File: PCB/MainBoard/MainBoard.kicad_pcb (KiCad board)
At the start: 2 copper layers, 100 x 100 mm, 73 parts, among them J10 Conn_01x06_Socket, J11 Conn_01x06_Socket, J12 Conn_01x04_Socket, J14 Conn_01x03_Socket, J17 Conn_01x02_Socket, J18 Conn_01x04_Socket, J19 Conn_01x04_Socket, J20 Conn_01x04_Socket, J21 Conn_01x02_Socket, J4 Conn_01x02_Socket, J5 Conn_01x03_Socket, J6 Conn_01x03_Socket, J7 Conn_01x03_Socket, J8 Conn_01x02_Socket, J9 Conn_01x02_Socket, SW1 SW_Push, U1 TPS56339DDC, U2 TPS56339DDC, U3 STM32F103C8Tx, U4 CD74HC00_N_14, U5 TPS56339DDC, U6 CD74HC00_N_14

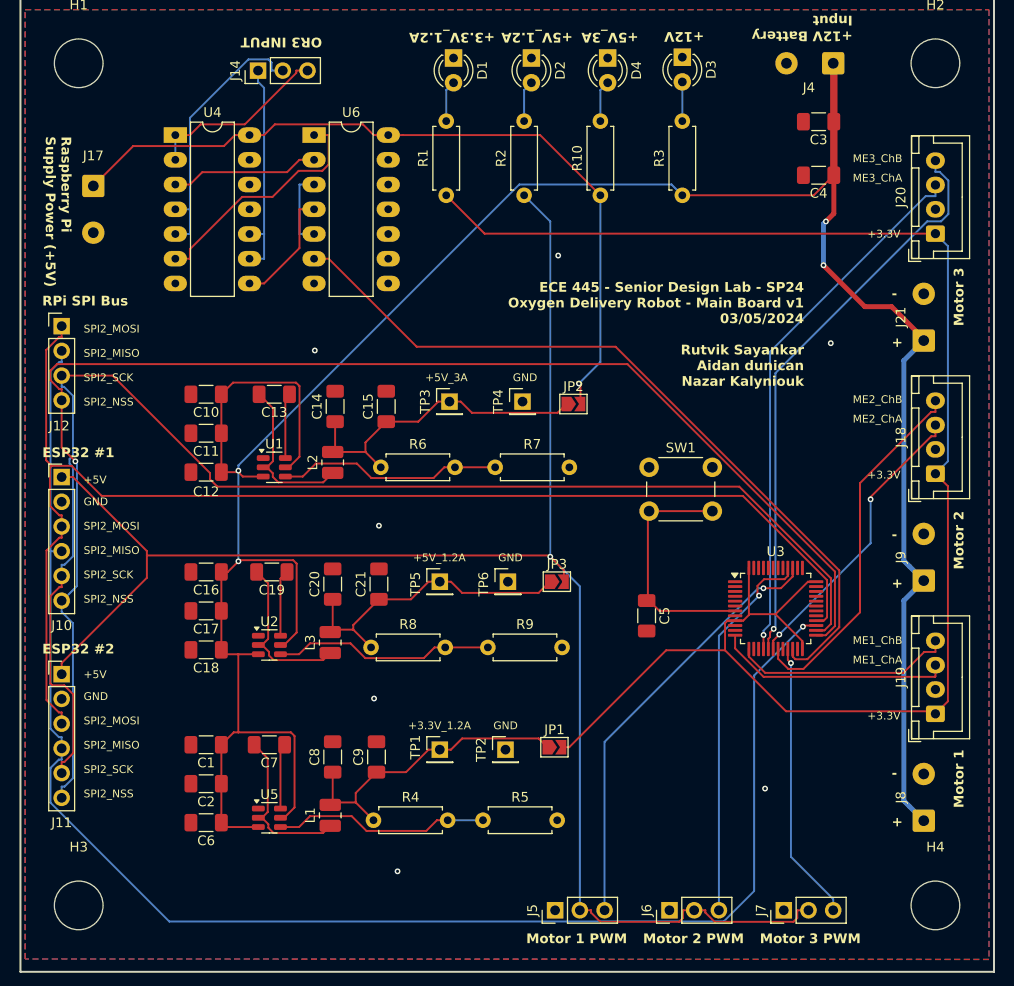
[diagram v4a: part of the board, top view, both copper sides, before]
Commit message: Updated PCB and passed DRC
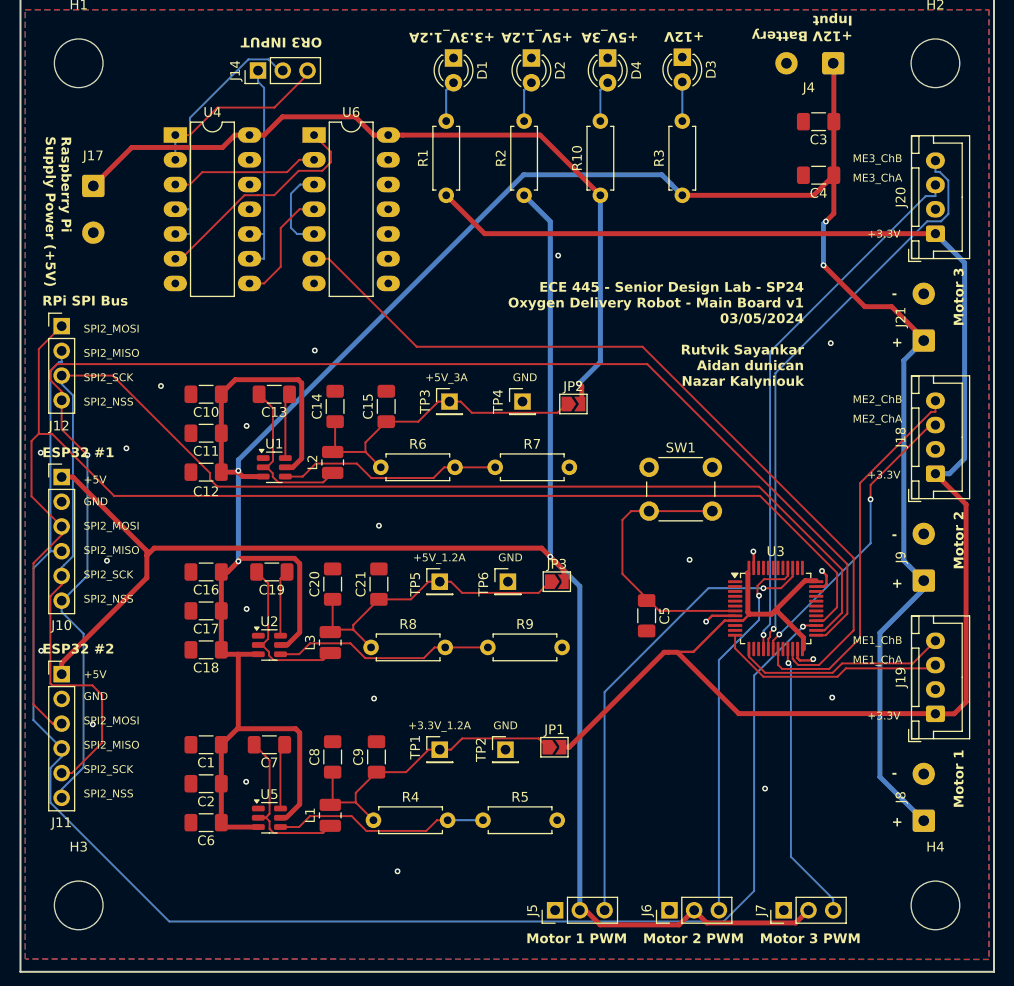
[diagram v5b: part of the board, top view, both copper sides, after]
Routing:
- net GND: track 0.00 -> 10.3 mm, vias 7 -> 22
- net +3.3V_1.2A: track 172.1 -> 181.5 mm
- net /SPI2_MOSI: track 133.8 -> 140.5 mm
- net /SPI2_SCK: track 139.9 -> 145.8 mm
- net +12V: track 269.4 -> 275.2 mm
- net /LimitSwitchORGates/OR3 Output: track 80.1 -> 84.6 mm
- net /SPI2_NSS: track 144.6 -> 148.3 mm
- net Net-(U3-NRST): track 25.2 -> 28.5 mm
- net Net-(J5-Pin_3): track 44.5 -> 47.5 mm
- net /ME2_ChB: track 37.5 -> 39.4 mm
- net Net-(U4-2Y): track 24.9 -> 23.6 mm
- net /SPI2_MISO: track 158.7 -> 159.8 mm
- net Net-(U6-1Y): track 8.08 -> 8.90 mm
- net +5V_3A: track 80.1 -> 80.8 mm
- net /ME1_ChA: track 24.3 -> 23.6 mm
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
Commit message: Updating main PCB for version 1.1
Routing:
- net +5V_1.2A: track 175.1 -> 177.5 mm
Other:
- board text added: "ECE 445 - Senior Design Lab - SP24 Oxygen Delivery Robot - Main Board v1.1 03/19/2024 Rutvik Sayankar Aidan Dunican Nazar Kalyniouk"
- board text added: "RPi Supply Power (+5V)"
- board text removed: "ECE 445 - Senior Design Lab - SP24 Oxygen Delivery Robot - Main Board v1 03/05/2024 Rutvik Sayankar Aidan dunican Nazar Kalyniouk"
- board text removed: "Raspberry Pi Supply Power (+5V)"
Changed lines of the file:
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@@
 			(at 0 -6 0)
 			(layer "F.SilkS")
+			(hide yes)
 			(effects
 				(font
@@
 			(at 0 -6 0)
 			(layer "F.SilkS")
+			(hide yes)
 			(effects
 				(font
@@
 			(at 0 -6 0)
 			(layer "F.SilkS")
+			(hide yes)
 			(effects
 				(font
@@
 		(tags "connector JST XH vertical")
 		(property "Reference" "J18"
-			(at 3.75 -3.55 -90)
+			(at 3.66 4.5 -90)
 			(layer "F.SilkS")
 			(effects
@@
 		(tags "connector JST XH vertical")
 		(property "Reference" "J20"
-			(at 3.75 -3.55 -90)
+			(at 3.5 4.5 -90)
 			(layer "F.SilkS")
 			(effects
@@
 			(at 0 -6 0)
 			(layer "F.SilkS")
+			(hide yes)
 			(effects
 				(font
@@
 		(tags "connector JST XH vertical")
 		(property "Reference" "J19"
-			(at 3.75 -3.55 -90)
+			(at 3.75 4.5 -90)
 			(layer "F.SilkS")
 			(effects
@@
 	)
 	(gr_text "-"
-		(at 192 102 0)
+		(at 193.483047 102.155047 90)
 		(layer "F.SilkS")
 		(effects
@@
 	)
 	(gr_text "ESP32 #2"
-		(at 104.75 113.75 0)
+		(at 103.5 118.5 -90)
 		(layer "F.SilkS")
 		(effects
@@
 		)
 	)
-	(gr_text "ECE 445 - Senior Design Lab - SP24\nOxygen Delivery Robot - Main Board v1\n03/05/2024\n\nRutvik Sayankar\nAidan dunican\nNazar Kalyniouk\n"
+	(gr_text "ECE 445 - Senior Design Lab - SP24\nOxygen Delivery Robot - Main Board v1.1\n03/19/2024\n\nRutvik Sayankar\nAidan Dunican\nNazar Kalyniouk\n"
 		(at 183 86.25 0)
 		(layer "F.SilkS")
@@
 	)
 	(gr_text "-"
-		(at 192 126.5 0)
+		(at 193.483047 126.655047 90)
 		(layer "F.SilkS")
 		(effects
@@
 		)
 	)
-	(gr_text "Raspberry Pi \nSupply Power (+5V)"
-		(at 105 60.5 270)
+	(gr_text "RPi Supply \nPower (+5V)"
+		(at 104.5 63.5 270)
 		(layer "F.SilkS")
 		(effects
@@
 	)
 	(gr_text "RPi SPI Bus\n"
-		(at 104.75 78 0)
+		(at 103.5 80 -90)
 		(layer "F.SilkS")
 		(effects
@@
 	)
 	(gr_text "-"
-		(at 192 77.25 0)
+		(at 193.483047 77.405047 90)
 		(layer "F.SilkS")
 		(effects
@@
 		)
 	)
+	(gr_text "+"
+		(at 112 66.5 0)
+		(layer "F.SilkS")
+		(effects
+			(font
+				(size 1 1)
+				(thickness 0.2)
+				(bold yes)
+			)
+			(justify left bottom)
+		)
+	)
 	(gr_text "+5V_3A"
 		(at 166 49.75 180)
@@
 		)
 	)
+	(gr_text "-"
+		(at 113 71 90)
+		(layer "F.SilkS")
+		(effects
+			(font
+				(size 1 1)
+				(thickness 0.2)
+				(bold yes)
+			)
+			(justify left bottom)
+		)
+	)
 	(gr_text "+3.3V_1.2A"
 		(at 142.3375 121.5 0)
@@
 	)
 	(gr_text "ESP32 #1"
-		(at 104.754762 93.578 0)
+		(at 103.5 99 -90)
 		(layer "F.SilkS")
 		(effects
@@
 		)
 	)
+	(gr_text "+"
+		(at 188.5 53.5 0)
+		(layer "F.SilkS")
+		(effects
+			(font
+				(size 1 1)
+				(thickness 0.2)
+				(bold yes)
+			)
+			(justify left bottom)
+		)
+	)
 	(gr_text "GND"
 		(at 109 98.5 0)
@@
 		)
 	)
+	(gr_text "-"
+		(at 179 52.5 180)
+		(layer "F.SilkS")
+		(effects
+			(font
+				(size 1 1)
+				(thickness 0.2)
+				(bold yes)
+			)
+			(justify left bottom)
+		)
+	)
 	(segment
 		(start 124.8935 121.35)
@@
 	)
 	(segment
-		(start 155.8983 60.375)
-		(end 141.7951 60.375)
-		(width 0.508)
-		(layer "F.Cu")
-		(net 16)
-	)
-	(segment
 		(start 136.9199 58.5)
 		(end 129.4201 58.5)
@@
 	(segment
 		(start 162.0833 66.56)
-		(end 155.8983 60.375)
+		(end 158.0233 62.5)
 		(width 0.508)
 		(layer "F.Cu")
@@
 	)
 	(segment
-		(start 138.7949 60.375)
-		(end 136.9199 58.5)
+		(start 141.7951 60.375)
+		(end 140.295 60.375)
 		(width 0.508)
 		(layer "F.Cu")
@@
 	)
 	(segment
-		(start 113.95 61.65)
-		(end 110 65.6)
+		(start 143.9201 62.5)
+		(end 141.7951 60.375)
 		(width 0.508)
 		(layer "F.Cu")
@@
 	)
 	(segment
-		(start 140.295 60.375)
-		(end 141.7951 60.375)
+		(start 138.7949 60.375)
+		(end 136.9199 58.5)
+		(width 0.508)
+		(layer "F.Cu")
+		(net 16)
+	)
+	(segment
+		(start 113.95 61.65)
+		(end 110 65.6)
 		(width 0.508)
 		(layer "F.Cu")
@@
 	)
 	(segment
+		(start 158.0233 62.5)
+		(end 143.9201 62.5)
+		(width 0.508)
+		(layer "F.Cu")
+		(net 16)
+	)
+	(segment
 		(start 127.5451 60.375)
 		(end 126.045 60.375)
@@
 	)
 	(segment
-		(start 115.5021 103.102)
-		(end 107.9001 95.5)
-		(width 0.508)
-		(layer "F.Cu")
-		(net 17)
-	)
-	(segment
-		(start 106.75 95.5)
-		(end 107.9001 95.5)
+		(start 118.92495 102.42495)
+		(end 115.5 99)
 		(width 0.508)
 		(layer "F.Cu")
@@
 	)
 	(segment
-		(start 106.75 114.5999)
-		(end 115.5021 105.8478)
-		(width 0.508)
-		(layer "F.Cu")
-		(net 17)
-	)
-	(segment
-		(start 115.5021 105.8478)
-		(end 115.5021 103.5541)
+		(start 112 99)
+		(end 108.5 95.5)
 		(width 0.508)
 		(layer "F.Cu")
@@
 	)
 	(segment
-		(start 116.2562 102.8)
-		(end 156.0494 102.8)
+		(start 119.8499 101.5)
+		(end 154.7494 101.5)
 		(width 0.508)
 		(layer "F.Cu")
@@
 	)
 	(segment
-		(start 115.5021 103.5541)
-		(end 115.5021 103.102)
+		(start 106.75 114.5999)
+		(end 119.8499 101.5)
 		(width 0.508)
 		(layer "F.Cu")
@@
 	)
 	(segment
-		(start 106.75 115.75)
-		(end 106.75 114.5999)
+		(start 158.346403 105.097003)
+		(end 158.346403 106.25)
 		(width 0.508)
 		(layer "F.Cu")
@@
 	)
 	(segment
-		(start 158.346403 105.097003)
-		(end 158.346403 106.25)
+		(start 156.9364 103.687)
+		(end 158.346403 105.097003)
 		(width 0.508)
 		(layer "F.Cu")
@@
 	)
 	(segment
-		(start 156.0494 102.8)
-		(end 156.9364 103.687)
+		(start 106.75 115.75)
+		(end 106.75 114.5999)
 		(width 0.508)
 		(layer "F.Cu")
@@
 	)
 	(segment
-		(start 156.9364 103.687)
-		(end 158.346403 105.097003)
+		(start 182.156 141.304)
+		(end 183.46 140)
 		(width 0.508)
 		(layer "F.Cu")
@@
 	)
 	(segment
-		(start 182.156 141.304)
-		(end 183.46 140)
+		(start 154.7494 101.5)
+		(end 156.9364 103.687)
+		(width 0.508)
+		(layer "F.Cu")
+		(net 17)
+	)
+	(segment
+		(start 108.5 95.5)
+		(end 106.75 95.5)
 		(width 0.508)
 		(layer "F.Cu")
@@
 	)
 	(segment
-		(start 115.5021 103.5541)
-		(end 116.2562 102.8)
+		(start 115.5 99)
+		(end 112 99)
 		(width 0.508)
 		(layer "F.Cu")

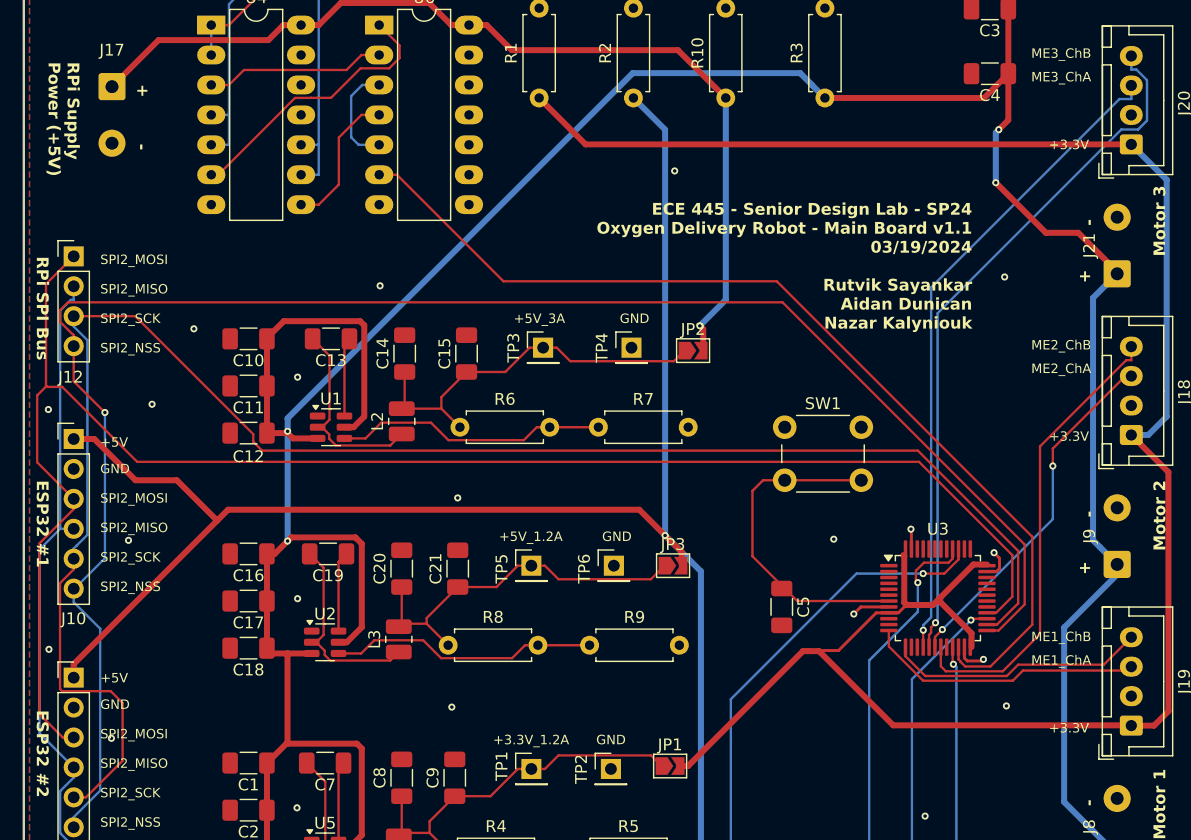
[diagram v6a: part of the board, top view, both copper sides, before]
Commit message: updating v1.1 with chamfered traces
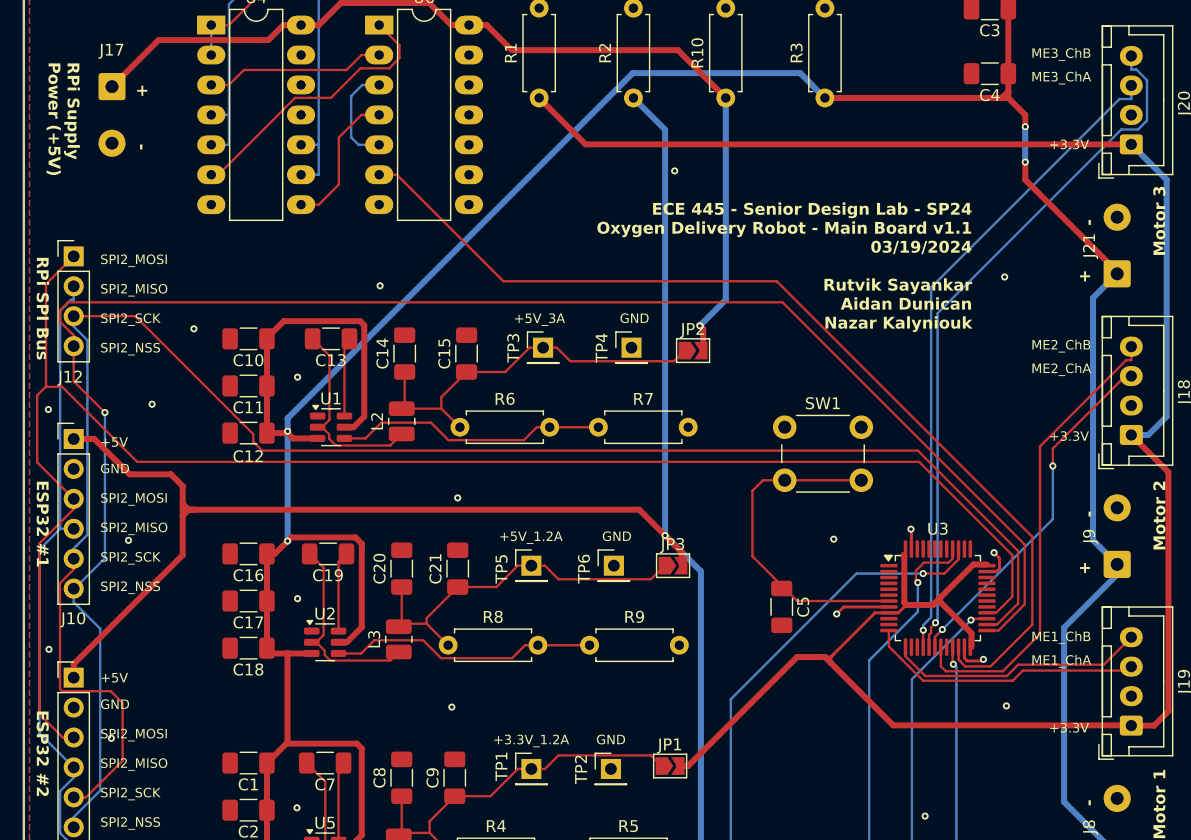
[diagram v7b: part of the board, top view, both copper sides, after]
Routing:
- net +12V: track 275.2 -> 273.1 mm
- net +5V_1.2A: track 177.5 -> 179.5 mm
- net GND: track 10.3 -> 11.8 mm

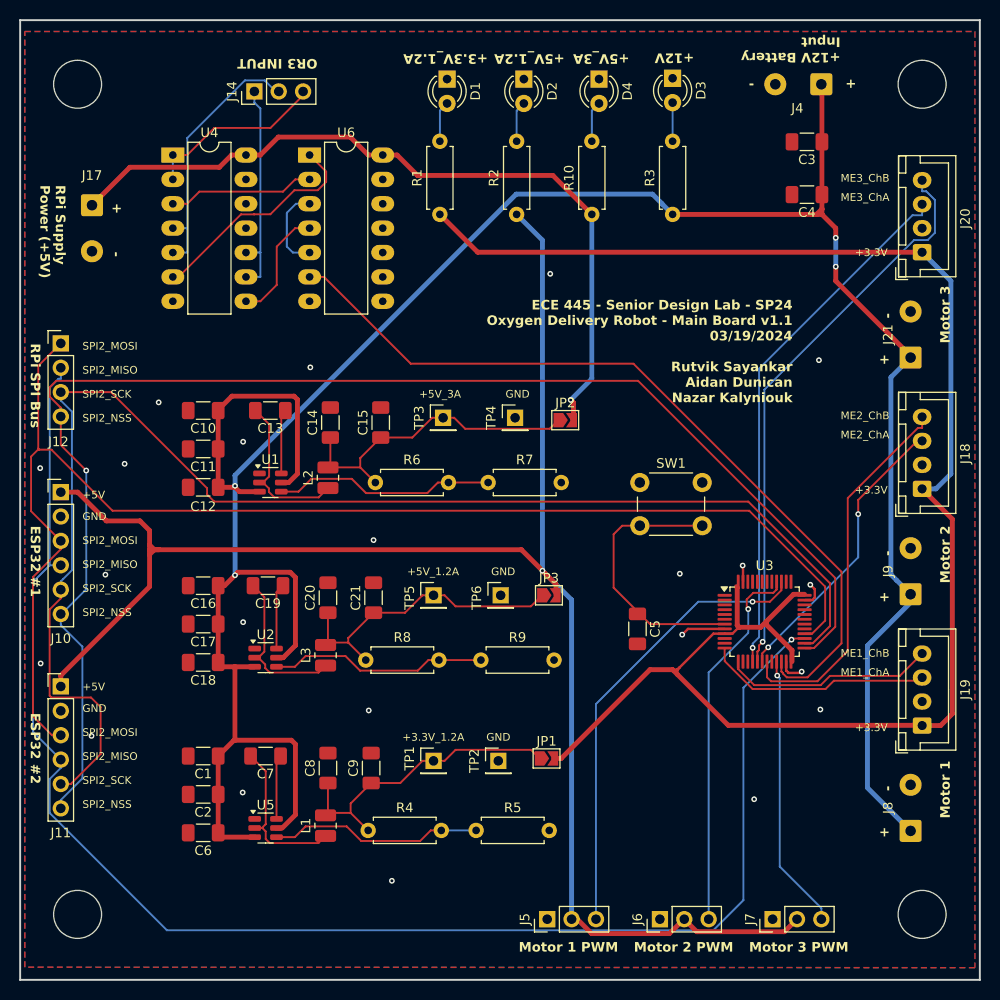
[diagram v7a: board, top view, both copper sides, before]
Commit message: updating PCB with new components and proper footprints, still need to fix footprint matching issue.
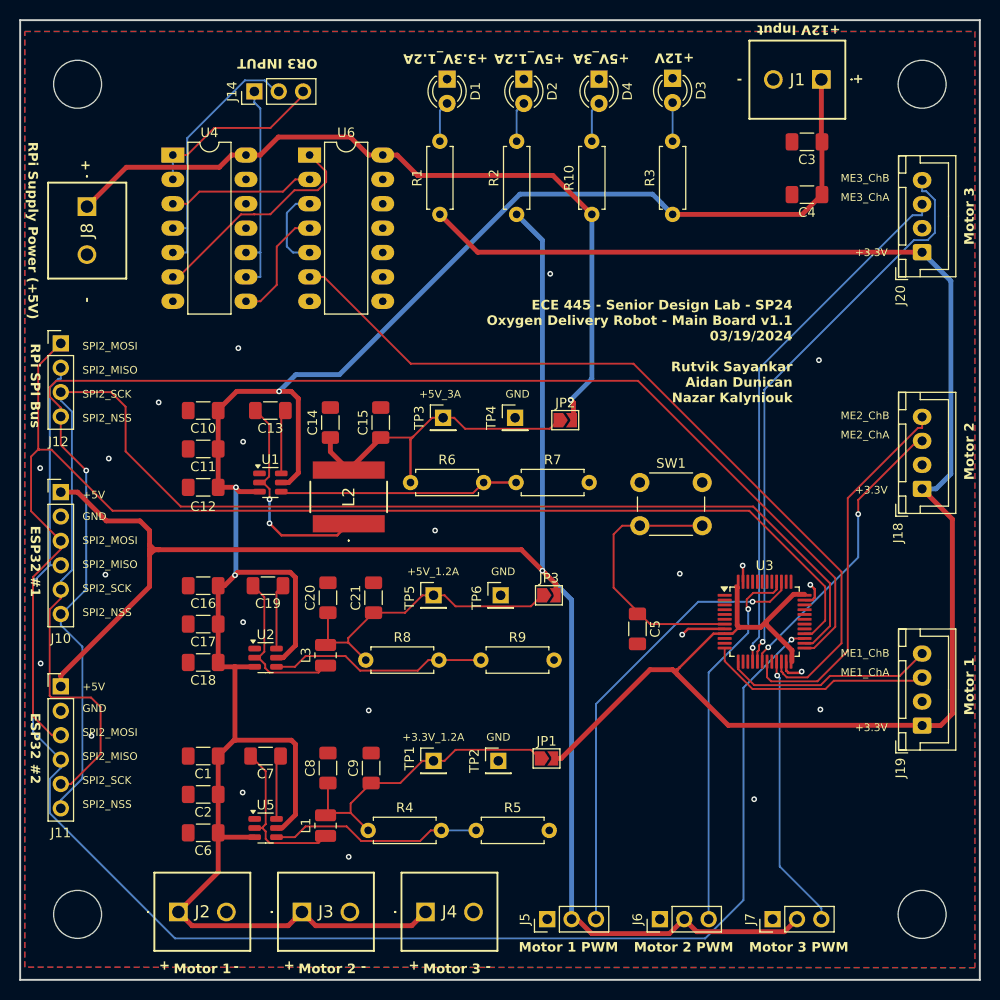
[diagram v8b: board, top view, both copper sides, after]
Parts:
- removed J17, J21, J9: Conn_01x02_Socket, Connector_Wire:SolderWire-0.5sqmm_1x02_P4.8mm_D0.9mm_OD2.3mm
- added J1: 5442170, ProjectLibrary:5442170, F.Cu at (186.0, 52.5)
- added J2: 5442170, ProjectLibrary:5442170, F.Cu at (119.0, 139.2)
- added J3: 5442170, ProjectLibrary:5442170, F.Cu at (131.9, 139.2)
- J4, J8: value Conn_01x02_Socket -> 5442170; footprint Connector_Wire:SolderWire-0.5sqmm_1x02_P4.8mm_D0.9mm_OD2.3mm -> ProjectLibrary:5442170
- L2: value 6.8u -> NRS8030T6R8MJGJ; footprint Inductor_SMD:L_1008_2520Metric -> ProjectLibrary:NRS8030T6R8MJGJ
- moved J8 107.7 mm to (109.5, 65.8), turned to -90 degrees
- moved J4 95.6 mm to (144.8, 139.2), turned to 0 degrees
- moved R6 3.66 mm to (143.2, 94.5)
- moved L2 2.95 mm to (136.8, 96.0)
- moved R7 2.91 mm to (154.2, 94.5)
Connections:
- J8 pad 1: +12V -> +5V_3A
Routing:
- net +12V: track 273.1 -> 226.7 mm, vias 4 -> 3
- net Net-(U1-SW): track 16.8 -> 22.5 mm, vias 0 -> 2
- net /SPI2_SCK: track 145.8 -> 148.2 mm
- net Net-(U1-FB): track 23.2 -> 25.0 mm
- net Net-(JP2-A): track 32.9 -> 34.0 mm
- net /SPI2_MISO: track 159.8 -> 160.5 mm
- net +5V_3A: track 80.8 -> 81.4 mm
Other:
- board text added: "+12V Input"
- board text removed: "+12V Battery Input"
